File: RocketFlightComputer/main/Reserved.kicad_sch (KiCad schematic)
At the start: 0 parts

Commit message: Camera and reserve
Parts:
- added TP1, TP2, TP3, TP4, TP5, TP6: TestPoint_2Pole, TestPoint:TestPoint_Bridge_Pitch2.54mm_Drill1.0mm, symbol Connector:TestPoint_2Pole
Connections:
- new net +3.3V: TP1.1
- new net +5V: TP3.1
- new net +7.5V: TP2.1
- new net GNDREF: TP1.2, TP2.2, TP3.2
- new net Reserve_RX1: TP4.2
- new net Reserve_RX2: TP5.2
- new net Reserve_RX3: TP6.2
- new net Reserve_TX1: TP4.1
- new net Reserve_TX2: TP5.1
- new net Reserve_TX3: TP6.1
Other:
- note added: "Power Reserve"
- note added: "UART Reserve"

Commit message: CID documentation and started the PCB editor process
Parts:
- TP1, TP2, TP3, TP4, TP5, TP6: footprint TestPoint:TestPoint_Bridge_Pitch2.54mm_Drill1.0mm -> TestPoint:TestPoint_2Pads_Pitch2.54mm_Drill0.8mm
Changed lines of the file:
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@@
 			)
 		)
-		(property "Footprint" "TestPoint:TestPoint_Bridge_Pitch2.54mm_Drill1.0mm"
+		(property "Footprint" "TestPoint:TestPoint_2Pads_Pitch2.54mm_Drill0.8mm"
 			(at 86.36 27.94 0)
 			(effects
@@
 			)
 		)
-		(property "Footprint" "TestPoint:TestPoint_Bridge_Pitch2.54mm_Drill1.0mm"
+		(property "Footprint" "TestPoint:TestPoint_2Pads_Pitch2.54mm_Drill0.8mm"
 			(at 34.29 62.23 0)
 			(effects
@@
 			)
 		)
-		(property "Footprint" "TestPoint:TestPoint_Bridge_Pitch2.54mm_Drill1.0mm"
+		(property "Footprint" "TestPoint:TestPoint_2Pads_Pitch2.54mm_Drill0.8mm"
 			(at 31.75 27.94 0)
 			(effects
@@
 			)
 		)
-		(property "Footprint" "TestPoint:TestPoint_Bridge_Pitch2.54mm_Drill1.0mm"
+		(property "Footprint" "TestPoint:TestPoint_2Pads_Pitch2.54mm_Drill0.8mm"
 			(at 58.42 27.94 0)
 			(effects
@@
 			)
 		)
-		(property "Footprint" "TestPoint:TestPoint_Bridge_Pitch2.54mm_Drill1.0mm"
+		(property "Footprint" "TestPoint:TestPoint_2Pads_Pitch2.54mm_Drill0.8mm"
 			(at 34.29 78.74 0)
 			(effects
@@
 			)
 		)
-		(property "Footprint" "TestPoint:TestPoint_Bridge_Pitch2.54mm_Drill1.0mm"
+		(property "Footprint" "TestPoint:TestPoint_2Pads_Pitch2.54mm_Drill0.8mm"
 			(at 34.29 71.12 0)
 			(effects

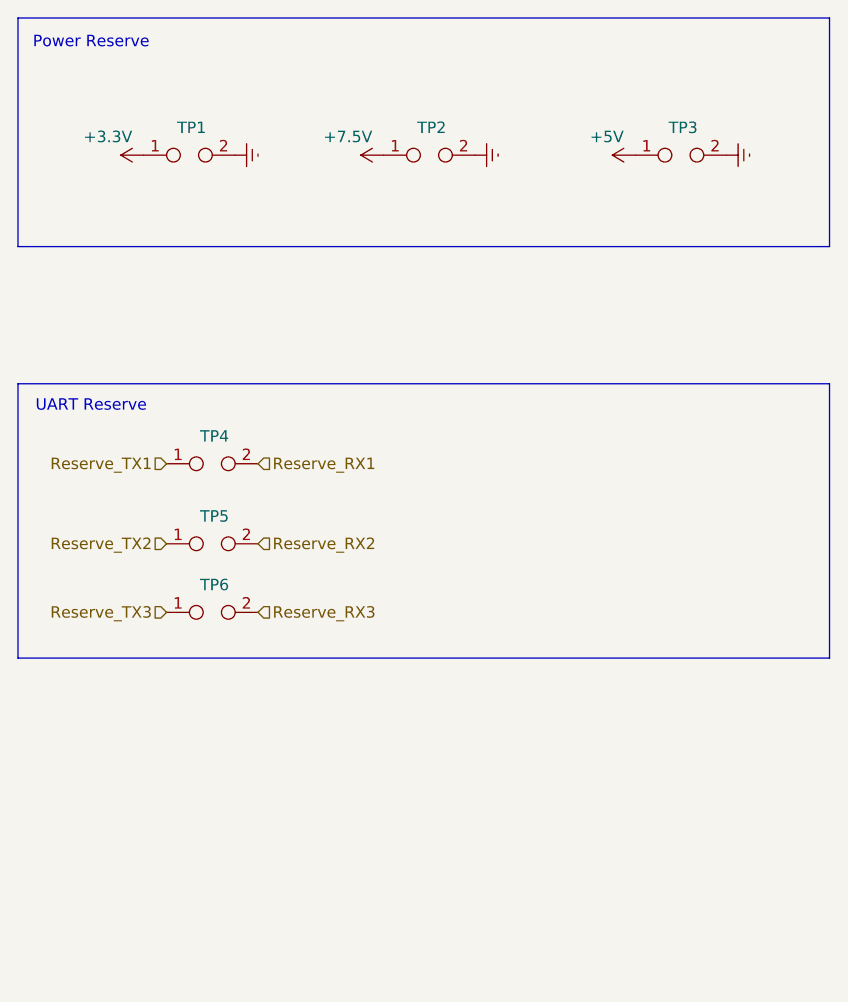
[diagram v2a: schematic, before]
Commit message: Layout of PCB mostly done
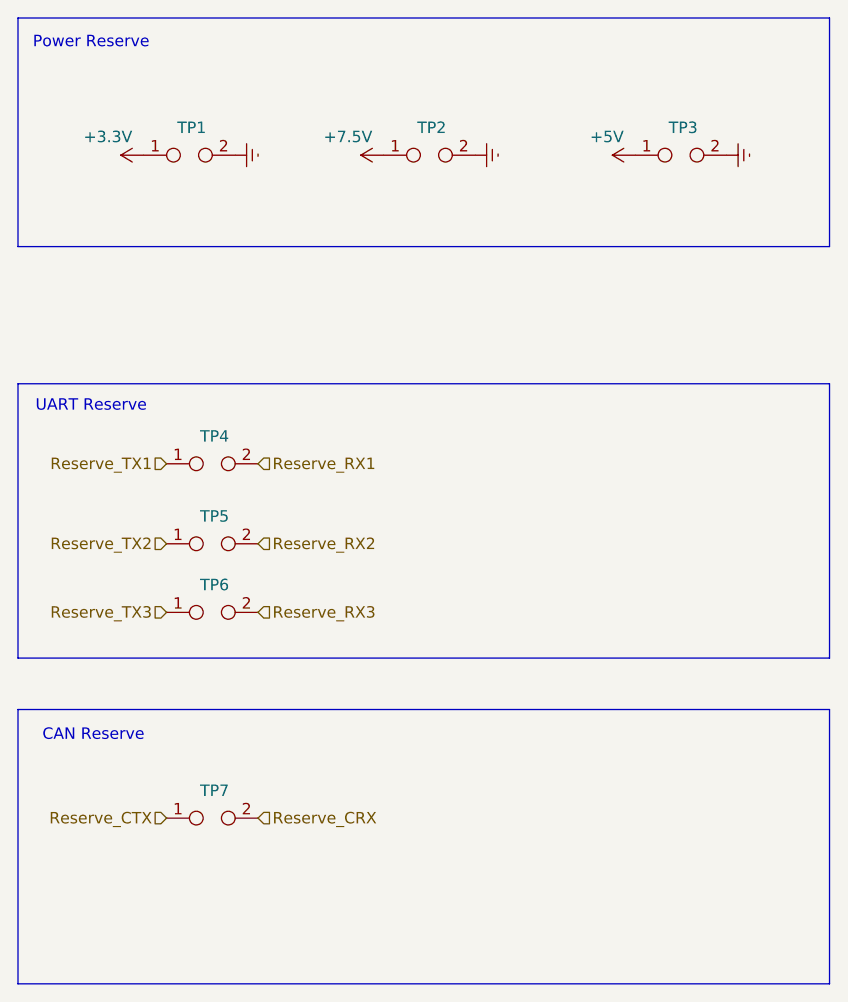
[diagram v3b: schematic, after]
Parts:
- added TP7: TestPoint_2Pole, TestPoint:TestPoint_2Pads_Pitch2.54mm_Drill0.8mm, symbol Connector:TestPoint_2Pole
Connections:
- new net Reserve_CRX: TP7.2
- new net Reserve_CTX: TP7.1
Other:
- note added: "CAN Reserve"
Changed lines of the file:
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@@
 	(paper "A4")
+	(rectangle
+		(start 12.7 89.535)
+		(end 102.87 120.015)
+		(stroke
+			(width 0)
+			(type default)
+		)
+		(fill
+			(type none)
+		)
+	)
 	(rectangle
 		(start 12.7 53.34)
@@
 		)
 	)
+	(text "CAN Reserve"
+		(exclude_from_sim no)
+		(at 21.082 92.456 0)
+		(effects
+			(font
+				(size 1.27 1.27)
+			)
+		)
+	)
 	(text "UART Reserve"
 		(exclude_from_sim no)
@@
 		)
 	)
+	(hierarchical_label "Reserve_CTX"
+		(shape input)
+		(at 29.21 101.6 180)
+		(fields_autoplaced yes)
+		(effects
+			(font
+				(size 1.27 1.27)
+			)
+			(justify right)
+		)
+	)
 	(hierarchical_label "Reserve_RX1"
 		(shape input)
 		(at 39.37 62.23 0)
+		(fields_autoplaced yes)
+		(effects
+			(font
+				(size 1.27 1.27)
+			)
+			(justify left)
+		)
+	)
+	(hierarchical_label "Reserve_CRX"
+		(shape input)
+		(at 39.37 101.6 0)
 		(fields_autoplaced yes)
 		(effects
@@
 					(unit 1)
 				)
+			)
+		)
+	)
+	(symbol
+		(lib_id "Connector:TestPoint_2Pole")
+		(at 34.29 101.6 0)
+		(unit 1)
+		(exclude_from_sim no)
+		(in_bom yes)
+		(on_board yes)
+		(dnp no)
+		(property "Reference" "TP7"
+			(at 34.544 98.552 0)
+			(effects
+				(font
+					(size 1.27 1.27)
+				)
+			)
+		)
+		(property "Value" "TestPoint_2Pole"
+			(at 34.29 99.06 0)
+			(effects
+				(font
+					(size 1.27 1.27)
+				)
+				(hide yes)
+			)
+		)
+		(property "Footprint" "TestPoint:TestPoint_2Pads_Pitch2.54mm_Drill0.8mm"
+			(at 34.29 101.6 0)
+			(effects
+				(font
+					(size 1.27 1.27)
+				)
+				(hide yes)
+			)
+		)
+		(property "Datasheet" "~"
+			(at 34.29 101.6 0)
+			(effects
+				(font
+					(size 1.27 1.27)
+				)
+				(hide yes)
+			)
+		)
+		(property "Description" "2-polar test point"
+			(at 34.29 101.6 0)
+			(effects
+				(font
+					(size 1.27 1.27)
+				)
+				(hide yes)
+			)
+		)
+		(pin "2"
+		)
+		(pin "1"
+		)
+		(instances
+			(project "main"
+				(path "/27195d1d-92b2-40df-ada5-3b20841577e7/d88c534c-db56-4afc-838f-d7c058479ac8"
+					(reference "TP7")
+					(unit 1)
+				)

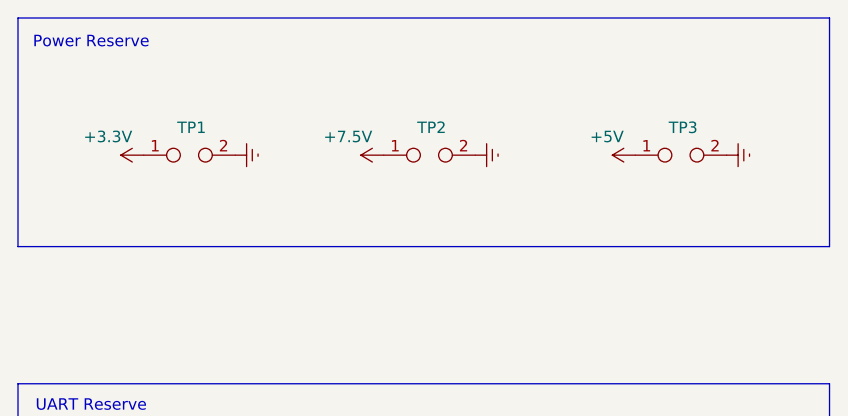
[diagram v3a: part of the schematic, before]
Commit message: Addition of teensy example and milestone on routing completed, missing a few components to connect
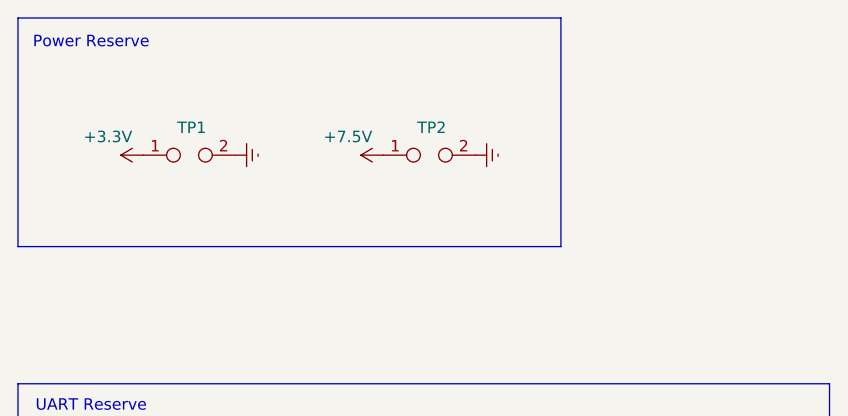
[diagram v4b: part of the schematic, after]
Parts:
- removed TP3: TestPoint_2Pole, TestPoint:TestPoint_2Pads_Pitch2.54mm_Drill0.8mm, symbol Connector:TestPoint_2Pole
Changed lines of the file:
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@@
 	(rectangle
 		(start 12.7 12.7)
-		(end 102.87 38.1)
+		(end 73.025 38.1)
 		(stroke
 			(width 0)
@@
 			)
 			(justify right)
-		)
-	)
-	(symbol
-		(lib_id "power:GNDREF")
-		(at 91.44 27.94 90)
-		(mirror x)
-		(unit 1)
-		(exclude_from_sim no)
-		(in_bom yes)
-		(on_board yes)
-		(dnp no)
-		(fields_autoplaced yes)
-		(property "Reference" "#PWR0144"
-			(at 97.79 27.94 0)
-			(effects
-				(font
-					(size 1.27 1.27)
-				)
-				(hide yes)
-			)
-		)
-		(property "Value" "GNDREF"
-			(at 95.25 27.305 90)
-			(effects
-				(font
-					(size 1.27 1.27)
-				)
-				(justify right)
-				(hide yes)
-			)
-		)
-		(property "Footprint" ""
-			(at 91.44 27.94 0)
-			(effects
-				(font
-					(size 1.27 1.27)
-				)
-				(hide yes)
-			)
-		)
-		(property "Datasheet" ""
-			(at 91.44 27.94 0)
-			(effects
-				(font
-					(size 1.27 1.27)
-				)
-				(hide yes)
-			)
-		)
-		(property "Description" ""
-			(at 91.44 27.94 0)
-			(effects
-				(font
-					(size 1.27 1.27)
-				)
-				(hide yes)
-			)
-		)
-		(pin "1"
-		)
-		(instances
-			(project "main"
-				(path "/27195d1d-92b2-40df-ada5-3b20841577e7/d88c534c-db56-4afc-838f-d7c058479ac8"
-					(reference "#PWR0144")
-					(unit 1)
-				)
-			)
-		)
-	)
-	(symbol
-		(lib_id "Connector:TestPoint_2Pole")
-		(at 86.36 27.94 0)
-		(unit 1)
-		(exclude_from_sim no)
-		(in_bom yes)
-		(on_board yes)
-		(dnp no)
-		(property "Reference" "TP3"
-			(at 86.614 24.892 0)
-			(effects
-				(font
-					(size 1.27 1.27)
-				)
-			)
-		)
-		(property "Value" "TestPoint_2Pole"
-			(at 86.36 25.4 0)
-			(effects
-				(font
-					(size 1.27 1.27)
-				)
-				(hide yes)
-			)
-		)
-		(property "Footprint" "TestPoint:TestPoint_2Pads_Pitch2.54mm_Drill0.8mm"
-			(at 86.36 27.94 0)
-			(effects
-				(font
-					(size 1.27 1.27)
-				)
-				(hide yes)
-			)
-		)
-		(property "Datasheet" "~"
-			(at 86.36 27.94 0)
-			(effects
-				(font
-					(size 1.27 1.27)
-				)
-				(hide yes)
-			)
-		)
-		(property "Description" "2-polar test point"
-			(at 86.36 27.94 0)
-			(effects
-				(font
-					(size 1.27 1.27)
-				)
-				(hide yes)
-			)
-		)
-		(pin "2"
-		)
-		(pin "1"
-		)
-		(instances
-			(project "main"
-				(path "/27195d1d-92b2-40df-ada5-3b20841577e7/d88c534c-db56-4afc-838f-d7c058479ac8"
-					(reference "TP3")
-					(unit 1)
-				)
-			)
 		)
 	)
@@
 					(unit 1)
 				)
-			)
-		)
-	)
-	(symbol
-		(lib_id "power:+3.3V")
-		(at 81.28 27.94 90)
-		(unit 1)
-		(exclude_from_sim no)
-		(in_bom yes)
-		(on_board yes)
-		(dnp no)
-		(property "Reference" "#PWR0118"
-			(at 85.09 27.94 0)
-			(effects
-				(font
-					(size 1.27 1.27)
-				)
-				(hide yes)
-			)
-		)
-		(property "Value" "+5V"
-			(at 80.01 25.908 90)
-			(effects
-				(font
-					(size 1.27 1.27)
-				)
-				(justify left)
-			)
-		)
-		(property "Footprint" ""
-			(at 81.28 27.94 0)
-			(effects
-				(font
-					(size 1.27 1.27)
-				)
-				(hide yes)
-			)
-		)
-		(property "Datasheet" ""
-			(at 81.28 27.94 0)
-			(effects
-				(font
-					(size 1.27 1.27)
-				)
-				(hide yes)
-			)
-		)
-		(property "Description" ""
-			(at 81.28 27.94 0)
-			(effects
-				(font
-					(size 1.27 1.27)
-				)
-				(hide yes)
-			)
-		)
-		(pin "1"
-		)
-		(instances
-			(project "main"
-				(path "/27195d1d-92b2-40df-ada5-3b20841577e7/d88c534c-db56-4afc-838f-d7c058479ac8"
-					(reference "#PWR0118")
-					(unit 1)
-				)

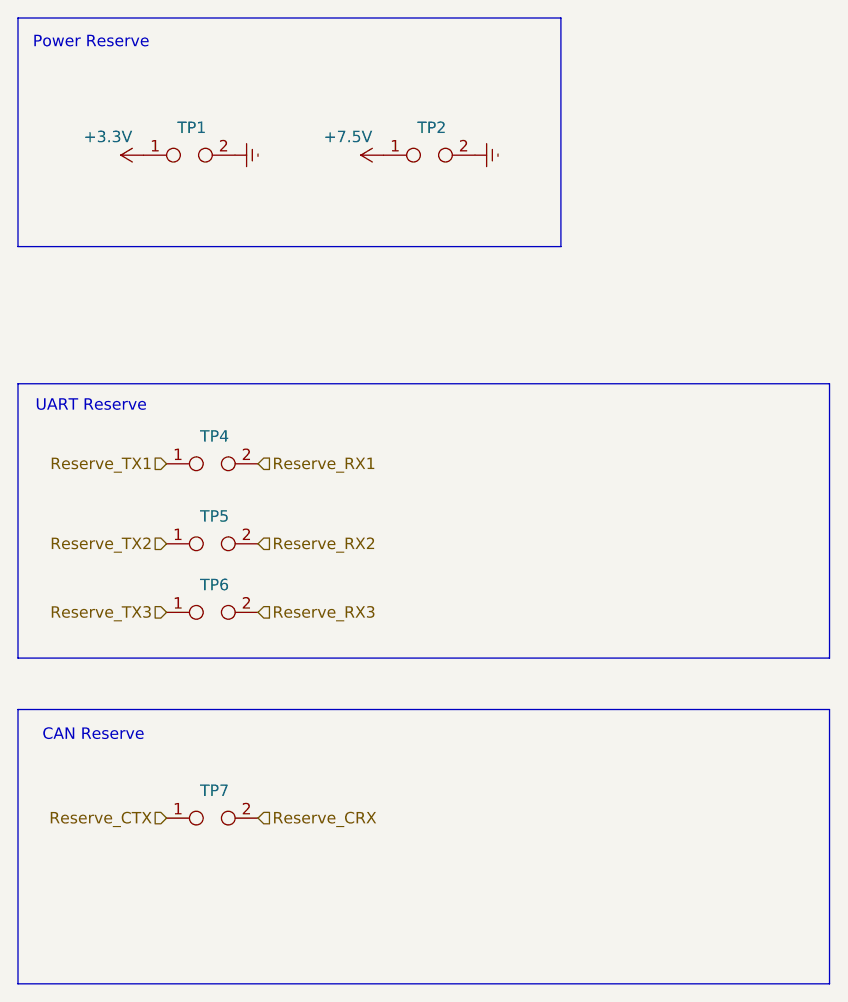
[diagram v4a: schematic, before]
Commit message: First iteration of layout finished, we could call this v0, congratulations! Need an expert to state if layer 4 and layer 3 interations are ok (pwm/ psram/i2c/uart vs power plane 7.5v and 3.3v )
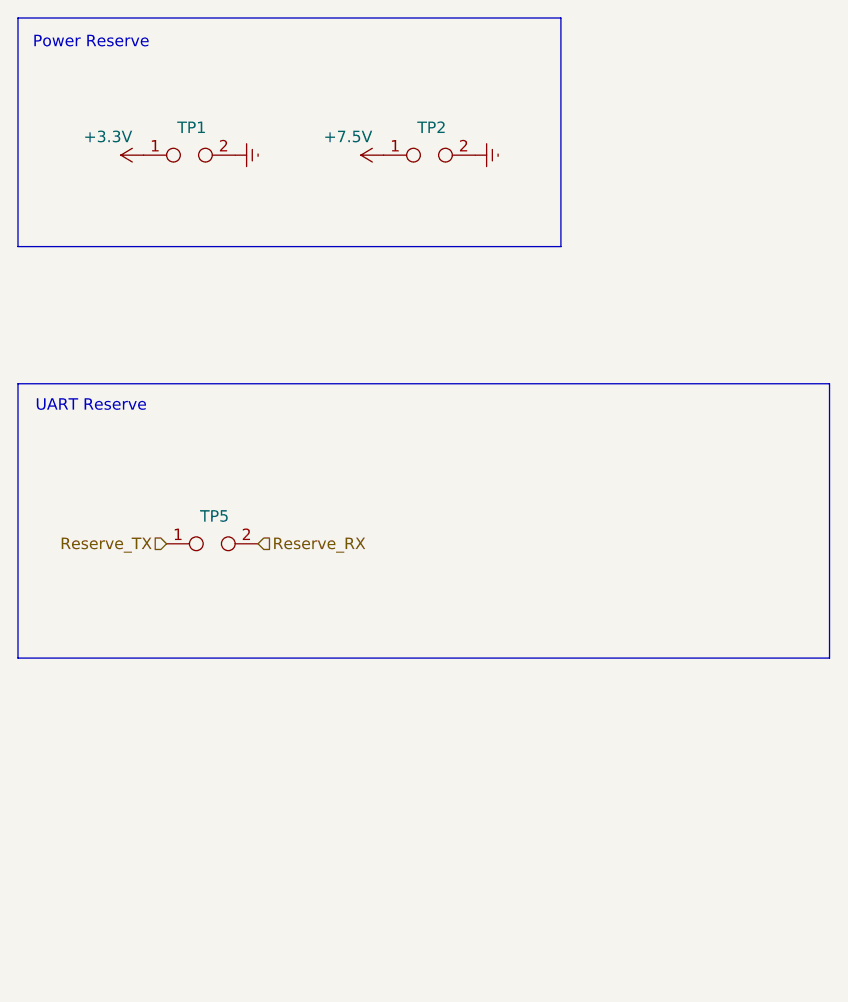
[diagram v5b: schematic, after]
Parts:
- removed TP4, TP6, TP7: TestPoint_2Pole, TestPoint:TestPoint_2Pads_Pitch2.54mm_Drill0.8mm, symbol Connector:TestPoint_2Pole
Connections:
- net Reserve_RX2 renamed Reserve_RX
- net Reserve_TX2 renamed Reserve_TX
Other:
- note removed: "CAN Reserve"

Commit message: Addition of all components in BOM, metal mounting plates, need to check psram if its ok for signals to pass under, all components need a double check
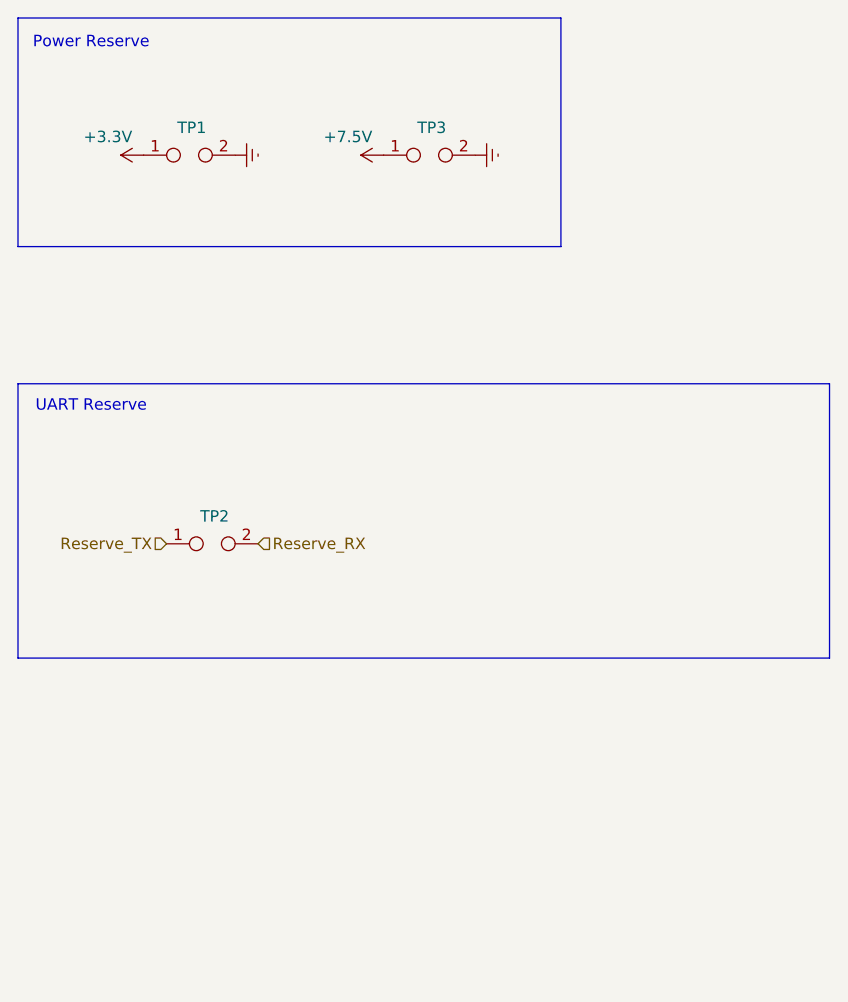
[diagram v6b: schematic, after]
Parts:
- renumbered TP5 to TP2, TP2 to TP3
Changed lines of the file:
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@@
 		(on_board yes)
 		(dnp no)
-		(property "Reference" "#PWR089"
+		(property "Reference" "#PWR0139"
 			(at 30.48 27.94 0)
 			(effects
@@
 			(project "main"
 				(path "/27195d1d-92b2-40df-ada5-3b20841577e7/d88c534c-db56-4afc-838f-d7c058479ac8"
-					(reference "#PWR089")
+					(reference "#PWR0139")
 					(unit 1)
 				)
@@
 		(on_board yes)
 		(dnp no)
-		(property "Reference" "#PWR0102"
+		(property "Reference" "#PWR0141"
 			(at 57.15 27.94 0)
 			(effects
@@
 			(project "main"
 				(path "/27195d1d-92b2-40df-ada5-3b20841577e7/d88c534c-db56-4afc-838f-d7c058479ac8"
-					(reference "#PWR0102")
+					(reference "#PWR0141")
 					(unit 1)
 				)
@@
 		(on_board yes)
 		(dnp no)
-		(property "Reference" "TP2"
+		(property "Reference" "TP3"
 			(at 58.674 24.892 0)
 			(effects
@@
 			(project "main"
 				(path "/27195d1d-92b2-40df-ada5-3b20841577e7/d88c534c-db56-4afc-838f-d7c058479ac8"
-					(reference "TP2")
+					(reference "TP3")
 					(unit 1)
 				)
@@
 		(dnp no)
 		(fields_autoplaced yes)
-		(property "Reference" "#PWR099"
+		(property "Reference" "#PWR0140"
 			(at 43.18 27.94 0)
 			(effects
@@
 			(project "main"
 				(path "/27195d1d-92b2-40df-ada5-3b20841577e7/d88c534c-db56-4afc-838f-d7c058479ac8"
-					(reference "#PWR099")
+					(reference "#PWR0140")
 					(unit 1)
 				)
@@
 		(dnp no)
 		(fields_autoplaced yes)
-		(property "Reference" "#PWR0103"
+		(property "Reference" "#PWR0142"
 			(at 69.85 27.94 0)
 			(effects
@@
 			(project "main"
 				(path "/27195d1d-92b2-40df-ada5-3b20841577e7/d88c534c-db56-4afc-838f-d7c058479ac8"
-					(reference "#PWR0103")
+					(reference "#PWR0142")
 					(unit 1)
 				)
@@
 		(on_board yes)
 		(dnp no)
-		(property "Reference" "TP5"
+		(property "Reference" "TP2"
 			(at 34.544 68.072 0)
 			(effects
@@
 			(project "main"
 				(path "/27195d1d-92b2-40df-ada5-3b20841577e7/d88c534c-db56-4afc-838f-d7c058479ac8"
-					(reference "TP5")
-					(unit 1)
-				)
+					(reference "TP2")
+					(unit 1)
+				)

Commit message: Last commit before changing bga to trace clearance of 6mils
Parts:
- TP1, TP2, TP3: now not fitted
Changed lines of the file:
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@@
 		(in_bom yes)
 		(on_board yes)
-		(dnp no)
+		(dnp yes)
 		(property "Reference" "TP1"
 			(at 32.004 24.892 0)
@@
 		(in_bom yes)
 		(on_board yes)
-		(dnp no)
+		(dnp yes)
 		(property "Reference" "TP3"
 			(at 58.674 24.892 0)
@@
 		(in_bom yes)
 		(on_board yes)
-		(dnp no)
+		(dnp yes)
 		(property "Reference" "TP2"
 			(at 34.544 68.072 0)
